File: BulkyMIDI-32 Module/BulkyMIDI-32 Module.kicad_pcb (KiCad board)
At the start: 2 copper layers, 97.8 x 97.8 mm, 31 parts, among them IC1 0.96_OLED, IC2 7406, IC3 I2C LC, J1 DC IN, J2 C64_IEC, J3 C64_IEC, J4 Faceplate, M1 Mounting, M2 Mounting, M3 Mounting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

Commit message: Schematic drafted
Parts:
- removed BZ1: Buzzer, Buzzers_Beepers:Buzzer_12x9.5RM7.6
- removed the REF** at (74.4, 82.5)
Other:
- board text added: "BulkyMIDI-32 Module (rev. A) github.com/tebl"
- board text removed: "1. Install smaller components (resistors, capacitors etc). 2. Install logic level converter module, trim down pins to size. 3. Install 7406 socket 4. Install 40 pin Raspberry Pi header if needed, adjust to match supporting standoffs oppsite. before soldering. 5. If installing 0.96" OLED here, link JP1 and JP2 to match OLED pinouts (1-2 when GND, VCC, SCL, SDA). Use female header for added height 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"
- board text removed: "INSTRUCTIONS"
- board text removed: "PI1541-II Module (rev. C) github.com/tebl Licensed under CERN OHL v.1.2"

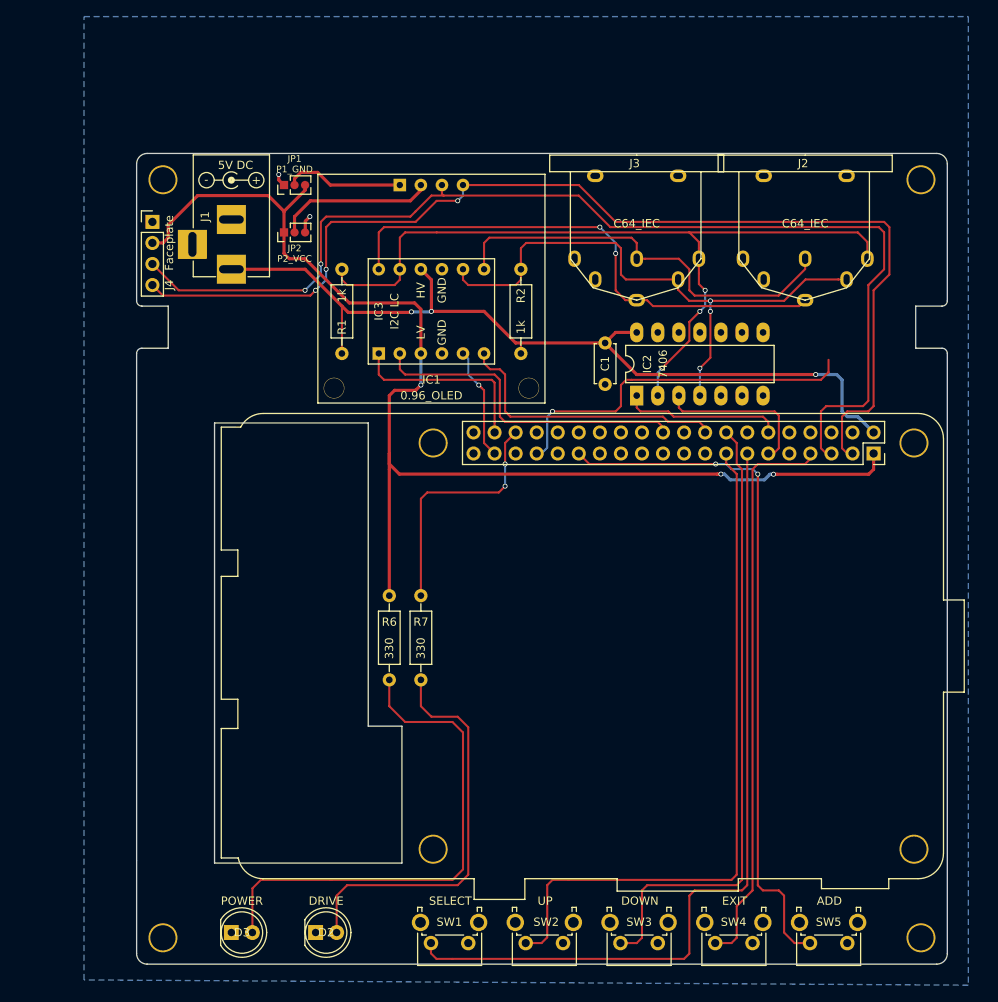
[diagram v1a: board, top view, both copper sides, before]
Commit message: Changed faceplate connector and PCB size
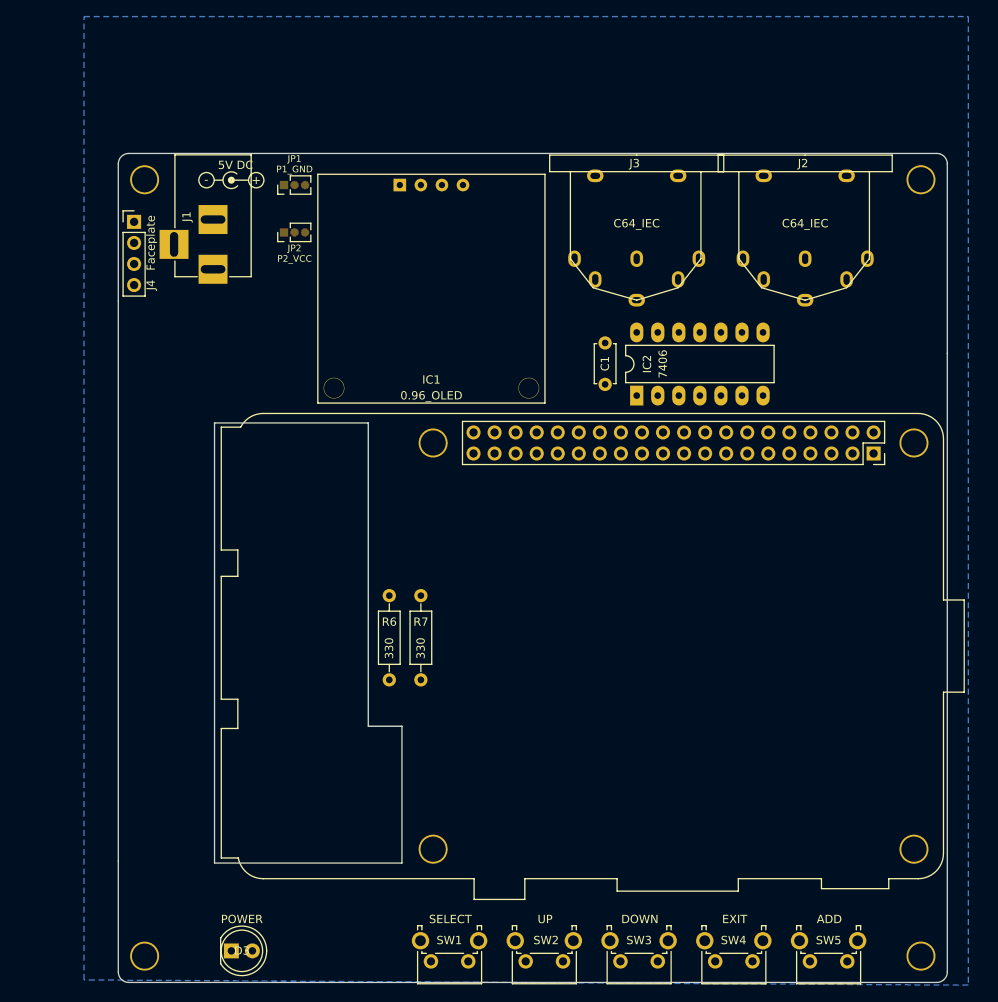
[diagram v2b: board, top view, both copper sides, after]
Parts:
- removed D2: DRIVE, LEDs:LED_D5.0mm
- removed IC3: I2C LC, IIC_4CH_Level_Converter:4CH_I2C_Level_Converter
- removed R1, R2: 1k, Resistors_THT:R_Axial_DIN0207_L6.3mm_D2.5mm_P10.16mm_Horizontal
- moved M1 3.13 mm to (73.4, 151.4)
- moved D3 2.21 mm to (83.8, 150.8)
- moved J4 2.21 mm to (72.1, 62.9)
- moved M2 2.21 mm to (167.0, 151.4)
- moved J1 2.21 mm to (81.6, 68.6)
- moved M4 2.21 mm to (73.4, 57.8)
- moved SW1 2.21 mm to (112.4, 152.1)
- moved SW2 2.21 mm to (123.8, 152.1)
- moved SW3 2.21 mm to (135.3, 152.1)
- moved SW4 2.21 mm to (146.7, 152.1)
- moved SW5 2.21 mm to (158.1, 152.1)
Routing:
- net +3V3: track 149.0 -> 0.00 mm, vias 3 -> 0
- net I2C_SCL: track 135.2 -> 0.63 mm, vias 2 -> 0
- net I2C_SDA: track 133.6 -> 0.00 mm, vias 3 -> 0
- net +5V: track 104.9 -> 0.00 mm, vias 3 -> 0
- net SW1: track 99.5 -> 0.00 mm
- net C64_DATA: track 95.9 -> 0.00 mm, vias 3 -> 0
- net SW5: track 84.0 -> 0.00 mm, vias 2 -> 0
- net SW2: track 83.9 -> 0.00 mm
- net SW3: track 76.0 -> 0.00 mm
- net C64_CLK: track 70.7 -> 0.00 mm, vias 3 -> 0
- net SW4: track 68.3 -> 0.00 mm
- net C64_RST: track 63.7 -> 0.00 mm, vias 2 -> 0
- net Net-(D3-Pad2): track 61.6 -> 0.00 mm
- net C64_ATN: track 50.2 -> 0.00 mm
- net Net-(D2-Pad2): track 49.1 -> 0.00 mm
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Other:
- board size 97.8 x 97.8 mm -> 100 x 100 mm

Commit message: Changed DIN to match
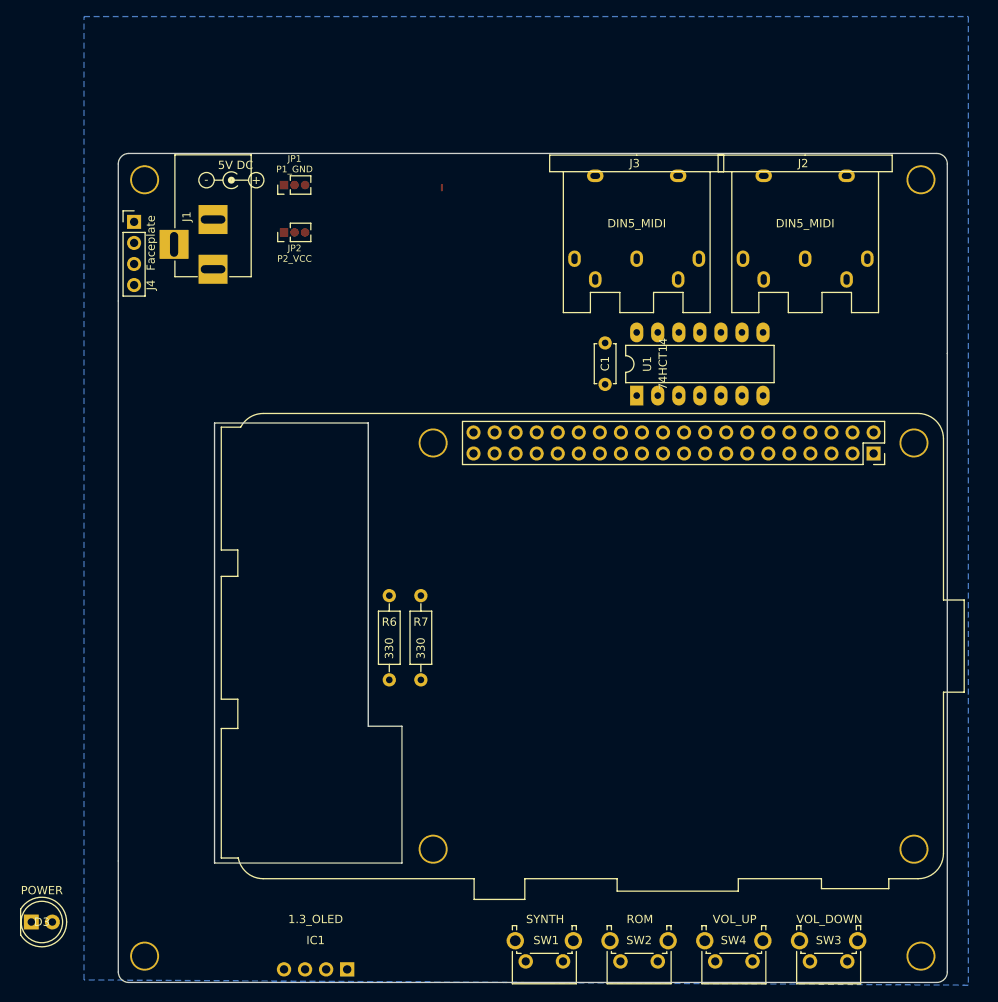
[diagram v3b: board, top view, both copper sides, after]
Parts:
- removed the SW1 at (112.4, 152.1)
- IC1: value 0.96_OLED -> 1.3_OLED; footprint i2c_oled:0.96_I2C_OLED -> i2c_oled:1.3_I2C_OLED_No_mounting
- J2, J3: value C64_IEC -> DIN5_MIDI; footprint C64_IEC:C64_IEC -> BulkyMIDI-32:DIN5_MIDI
- SW1: renamed from SW2; value UP -> SYNTH
- SW2: renamed from SW3; value DOWN -> ROM
- SW3: renamed from SW5; value ADD -> VOL_DOWN
- SW4: value EXIT -> VOL_UP
- U1: renamed from IC2; value 7406 -> 74HCT14
- moved IC1 95.6 mm to (94.0, 153.0), turned to 180 degrees
- moved D3 24.4 mm to (59.7, 147.3)

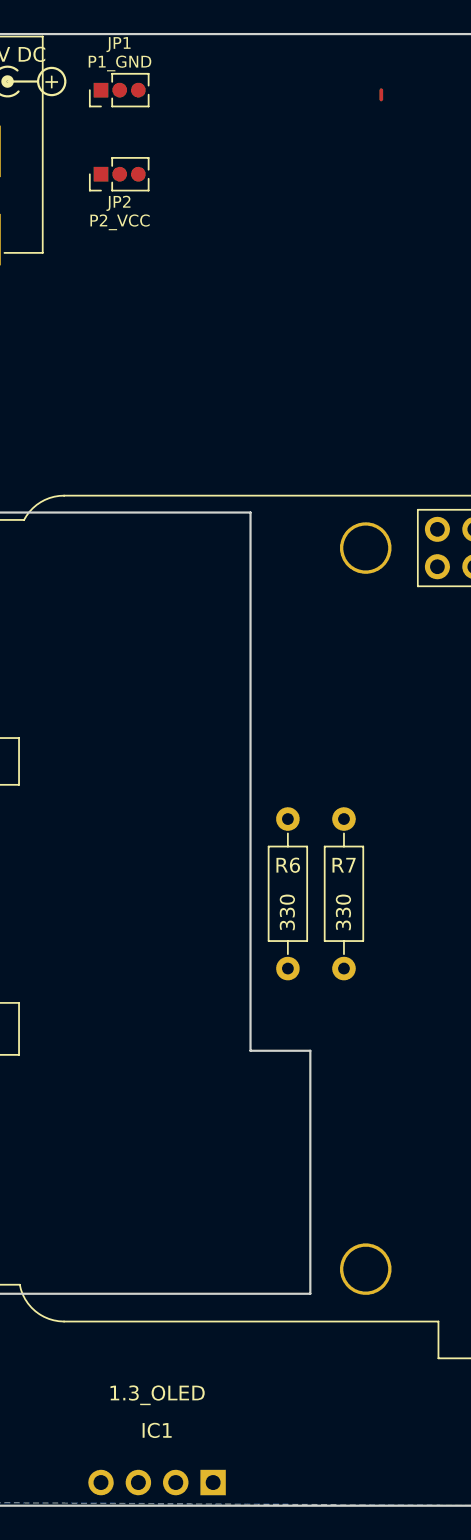
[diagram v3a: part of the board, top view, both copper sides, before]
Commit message: Moved display
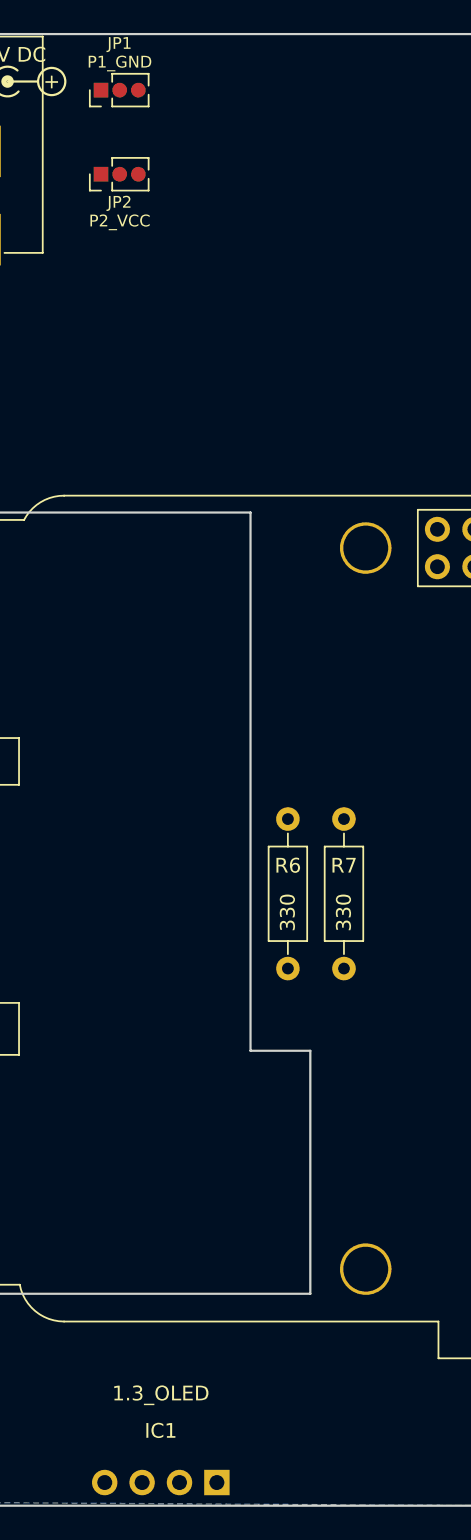
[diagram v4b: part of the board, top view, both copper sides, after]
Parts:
- moved IC1 0.25 mm to (94.2, 153.0)
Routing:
- net I2C_SCL: track 0.63 -> 0.00 mm

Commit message: Moved JP1, JP2
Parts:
- moved JP1 89.1 mm to (95.9, 147.3)
- moved JP2 83.2 mm to (90.8, 147.3)
- moved D3 13.3 mm to (72.4, 143.5)
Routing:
- net +3V3: track 0.00 -> 10.7 mm
- net Net-(IC1-Pad2): track 0.00 -> 8.25 mm
- net Net-(IC1-Pad1): track 0.00 -> 6.08 mm
- net GND: track 0.00 -> 2.54 mm, vias 0 -> 1
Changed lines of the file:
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@@
     (thickness 1.6)
     (drawings 25)
-    (tracks 0)
+    (tracks 17)
     (zones 0)
     (modules 24)
@@
     (descr "Through hole straight pin header, 1x04, 2.54mm pitch, single row")
     (tags "Through hole pin header THT 1x04 2.54mm single row")
-    (fp_text reference IC1 (at 0 3.505 180) (layer F.SilkS)
-      (effects (font (size 1 1) (thickness 0.15)))
-    )
-    (fp_text value 1.3_OLED (at 0 6.045) (layer F.SilkS)
-      (effects (font (size 1 1) (thickness 0.15)))
-    )
+    (fp_text reference IC1 (at 10.795 8.89 180) (layer F.SilkS)
+      (effects (font (size 0.8 0.8) (thickness 0.1)))
+    )
+    (fp_text value 1.3_OLED (at 11.049 7.62) (layer F.SilkS)
+      (effects (font (size 0.8 0.8) (thickness 0.1)))
+    )
+    (fp_text user %R (at 0 23.495 180) (layer F.Fab)
+      (effects (font (size 1 1) (thickness 0.15)))
+    )
+    (fp_line (start 7 25.95) (end 7 31.35) (layer Dwgs.User) (width 0.15))
+    (fp_line (start -7 25.95) (end -7 31.35) (layer Dwgs.User) (width 0.15))
+    (fp_line (start 17.5 31.7) (end 17.5 -1.3) (layer F.Fab) (width 0.15))
+    (fp_line (start -17.5 31.7) (end 17.5 31.7) (layer F.Fab) (width 0.15))
+    (fp_line (start -17.5 -1.3) (end -17.5 31.7) (layer F.Fab) (width 0.15))
+    (fp_line (start -17.5 -1.3) (end 17.5 -1.3) (layer F.Fab) (width 0.15))
+    (fp_line (start -16.51 25.95) (end 16.51 25.95) (layer Dwgs.User) (width 0.15))
+    (fp_line (start 16.51 25.95) (end 16.51 3.175) (layer Dwgs.User) (width 0.15))
+    (fp_line (start 16.51 3.175) (end -16.51 3.175) (layer Dwgs.User) (width 0.15))
     (fp_line (start -16.51 3.175) (end -16.51 25.95) (layer Dwgs.User) (width 0.15))
-    (fp_line (start 16.51 3.175) (end -16.51 3.175) (layer Dwgs.User) (width 0.15))
-    (fp_line (start 16.51 25.95) (end 16.51 3.175) (layer Dwgs.User) (width 0.15))
-    (fp_line (start -16.51 25.95) (end 16.51 25.95) (layer Dwgs.User) (width 0.15))
-    (fp_line (start -17.5 -1.3) (end 17.5 -1.3) (layer F.Fab) (width 0.15))
-    (fp_line (start -17.5 -1.3) (end -17.5 31.7) (layer F.Fab) (width 0.15))
-    (fp_line (start -17.5 31.7) (end 17.5 31.7) (layer F.Fab) (width 0.15))
-    (fp_line (start 17.5 31.7) (end 17.5 -1.3) (layer F.Fab) (width 0.15))
-    (fp_line (start -7 25.95) (end -7 31.35) (layer Dwgs.User) (width 0.15))
-    (fp_line (start 7 25.95) (end 7 31.35) (layer Dwgs.User) (width 0.15))
-    (fp_text user %R (at 0 23.495 180) (layer F.Fab)
-      (effects (font (size 1 1) (thickness 0.15)))
-    )
+    (pad 4 thru_hole circle (at 3.81 0 180) (size 1.7272 1.7272) (drill 1.016) (layers *.Cu *.Mask)
+      (net 21 I2C_SDA))
+    (pad 3 thru_hole circle (at 1.27 0 180) (size 1.7272 1.7272) (drill 1.016) (layers *.Cu *.Mask)
+      (net 18 I2C_SCL))
+    (pad 2 thru_hole circle (at -1.27 0 180) (size 1.7272 1.7272) (drill 1.016) (layers *.Cu *.Mask)
+      (net 5 "Net-(IC1-Pad2)"))
     (pad 1 thru_hole rect (at -3.81 0 180) (size 1.7272 1.7272) (drill 1.016) (layers *.Cu *.Mask)
       (net 22 "Net-(IC1-Pad1)"))
-    (pad 2 thru_hole circle (at -1.27 0 180) (size 1.7272 1.7272) (drill 1.016) (layers *.Cu *.Mask)
-      (net 5 "Net-(IC1-Pad2)"))
-    (pad 3 thru_hole circle (at 1.27 0 180) (size 1.7272 1.7272) (drill 1.016) (layers *.Cu *.Mask)
-      (net 18 I2C_SCL))
-    (pad 4 thru_hole circle (at 3.81 0 180) (size 1.7272 1.7272) (drill 1.016) (layers *.Cu *.Mask)
-      (net 21 I2C_SDA))
   )
   (module BulkyMIDI-32:DIN5_MIDI (layer F.Cu)
@@
   )
   (module wire_pads:OLED_SEL (layer F.Cu)
-    (at 90.17 64.135 90)
+    (at 90.805 147.32 90)
     (descr "Through hole straight pin header, 1x03, 1.27mm pitch, single row")
     (tags "Through hole pin header THT 1x03 1.27mm single row")
-    (fp_text reference JP2 (at -1.905 1.27) (layer F.SilkS)
+    (fp_text reference JP2 (at 3.175 1.27 180) (layer F.SilkS)
       (effects (font (size 0.8 0.8) (thickness 0.1)))
     )
-    (fp_text value P2_VCC (at -3.175 1.27 180) (layer F.SilkS)
+    (fp_text value P2_VCC (at 1.905 1.27 180) (layer F.SilkS)
       (effects (font (size 0.8 0.8) (thickness 0.1)))
     )
@@
     (fp_line (start -1.11 0) (end -1.11 -0.76) (layer F.SilkS) (width 0.12))
     (fp_line (start -1.11 -0.76) (end 0 -0.76) (layer F.SilkS) (width 0.12))
-    (fp_text user %R (at 0 -1.905 270) (layer F.Fab)
+    (fp_text user %R (at 3.175 1.27) (layer F.Fab)
       (effects (font (size 1 1) (thickness 0.15)))
     )
@@
   )
   (module LEDs:LED_D5.0mm (layer F.Cu)
-    (at 59.69 147.32)
+    (at 72.39 143.51)
     (descr "LED, diameter 5.0mm, 2 pins, http://cdn-reichelt.de/documents/datenblatt/A500/LL-504BC2E-009.pdf")
     (tags "LED diameter 5.0mm 2 pins")
@@
   )
   (module wire_pads:OLED_SEL (layer F.Cu)
-    (at 90.17 58.42 90)
+    (at 95.885 147.32 90)
     (descr "Through hole straight pin header, 1x03, 1.27mm pitch, single row")
     (tags "Through hole pin header THT 1x03 1.27mm single row")
@@
     (fp_line (start 1.05 -0.635) (end 1.05 3.175) (layer F.Fab) (width 0.1))
     (fp_line (start -0.525 -0.635) (end 1.05 -0.635) (layer F.Fab) (width 0.1))
-    (fp_text user %R (at 0 -1.905 270) (layer F.Fab)
+    (fp_text user %R (at 3.175 1.27) (layer F.Fab)
       (effects (font (size 1 1) (thickness 0.15)))
     )
@@
   (gr_line (start 71.45 154.61) (end 168.91 154.61) (angle 90) (layer Edge.Cuts) (width 0.15))
   (gr_arc (start 71.45 153.34) (end 71.45 154.61) (angle 90) (layer Edge.Cuts) (width 0.15))
+  (via (at 94.615 147.32) (size 0.6) (drill 0.4) (layers F.Cu B.Cu) (net 1))
+  (segment (start 93.345 147.32) (end 94.615 147.32) (width 0.25) (layer F.Cu) (net 1))
+  (segment (start 95.885 147.32) (end 94.615 147.32) (width 0.25) (layer F.Cu) (net 1))
+  (segment (start 90.805 147.32) (end 90.805 146.05) (width 0.25) (layer F.Cu) (net 2))
+  (segment (start 90.805 146.05) (end 91.44 145.415) (width 0.25) (layer F.Cu) (net 2))
+  (segment (start 91.44 145.415) (end 97.79 145.415) (width 0.25) (layer F.Cu) (net 2))
+  (segment (start 98.425 146.05) (end 98.425 147.32) (width 0.25) (layer F.Cu) (net 2))
+  (segment (start 97.79 145.415) (end 98.425 146.05) (width 0.25) (layer F.Cu) (net 2))
+  (segment (start 95.504 151.384) (end 95.504 153.035) (width 0.25) (layer F.Cu) (net 5))
+  (segment (start 92.075 147.32) (end 92.075 147.955) (width 0.25) (layer F.Cu) (net 5))
+  (segment (start 92.71 148.59) (end 94.615 148.59) (width 0.25) (layer F.Cu) (net 5))
+  (segment (start 92.075 147.955) (end 92.71 148.59) (width 0.25) (layer F.Cu) (net 5))
+  (segment (start 95.504 149.479) (end 95.504 151.384) (width 0.25) (layer F.Cu) (net 5))
+  (segment (start 94.615 148.59) (end 95.504 149.479) (width 0.25) (layer F.Cu) (net 5))
+  (segment (start 97.155 148.59) (end 97.155 147.32) (width 0.25) (layer F.Cu) (net 22))
+  (segment (start 98.044 149.479) (end 97.155 148.59) (width 0.25) (layer F.Cu) (net 22))
+  (segment (start 98.044 153.035) (end 98.044 149.479) (width 0.25) (layer F.Cu) (net 22))
   (zone (net 1) (net_name GND) (layer B.Cu) (hatch edge 0.508)
     (connect_pads (clearance 0.508))
